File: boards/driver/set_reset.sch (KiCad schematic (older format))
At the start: 20 parts, among them Q86 MMBT2222, Q87 MMBT2907, Q88 MMBT2222, Q89 MMBT2222

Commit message: Driver board: a bit more schematic work and some initial footprint selections
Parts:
- R215, R216, R217, R218, R219, R220, R221: footprint Resistor_SMD:R_1206_3216Metric -> Resistor_SMD:R_0603_1608Metric
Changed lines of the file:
@@
 F 0 "R215" V 3795 3550 50  0000 C CNN
 F 1 "500" V 3886 3550 50  0000 C CNN
-F 2 "Resistor_SMD:R_1206_3216Metric" V 4040 3540 50  0001 C CNN
+F 2 "Resistor_SMD:R_0603_1608Metric" V 4040 3540 50  0001 C CNN
 F 3 "~" H 4000 3550 50  0001 C CNN
 	1    4000 3550
@@
 F 0 "R216" V 4595 3300 50  0000 C CNN
 F 1 "1k" V 4686 3300 50  0000 C CNN
-F 2 "Resistor_SMD:R_1206_3216Metric" V 4840 3290 50  0001 C CNN
+F 2 "Resistor_SMD:R_0603_1608Metric" V 4840 3290 50  0001 C CNN
 F 3 "~" H 4800 3300 50  0001 C CNN
 	1    4800 3300
@@
 F 0 "R217" H 5068 2946 50  0000 L CNN
 F 1 "5.1k" H 5068 2855 50  0000 L CNN
-F 2 "Resistor_SMD:R_1206_3216Metric" V 5040 2890 50  0001 C CNN
+F 2 "Resistor_SMD:R_0603_1608Metric" V 5040 2890 50  0001 C CNN
 F 3 "~" H 5000 2900 50  0001 C CNN
 	1    5000 2900
@@
 F 0 "R219" H 5968 2896 50  0000 L CNN
 F 1 "27" H 5968 2805 50  0000 L CNN
-F 2 "Resistor_SMD:R_1206_3216Metric" V 5940 2840 50  0001 C CNN
+F 2 "Resistor_SMD:R_0603_1608Metric" V 5940 2840 50  0001 C CNN
 F 3 "~" H 5900 2850 50  0001 C CNN
 	1    5900 2850
@@
 F 0 "R218" H 5118 4196 50  0000 L CNN
 F 1 "5.1k" H 5118 4105 50  0000 L CNN
-F 2 "Resistor_SMD:R_1206_3216Metric" V 5090 4140 50  0001 C CNN
+F 2 "Resistor_SMD:R_0603_1608Metric" V 5090 4140 50  0001 C CNN
 F 3 "~" H 5050 4150 50  0001 C CNN
 	1    5050 4150
@@
 F 0 "R220" H 6718 4296 50  0000 L CNN
 F 1 "NOM" H 6718 4205 50  0000 L CNN
-F 2 "Resistor_SMD:R_1206_3216Metric" V 6690 4240 50  0001 C CNN
+F 2 "Resistor_SMD:R_0603_1608Metric" V 6690 4240 50  0001 C CNN
 F 3 "~" H 6650 4250 50  0001 C CNN
 	1    6650 4250
@@
 F 0 "R221" H 7368 4146 50  0000 L CNN
 F 1 "NOM" H 7368 4055 50  0000 L CNN
-F 2 "Resistor_SMD:R_1206_3216Metric" V 7340 4090 50  0001 C CNN
+F 2 "Resistor_SMD:R_0603_1608Metric" V 7340 4090 50  0001 C CNN
 F 3 "~" H 7300 4100 50  0001 C CNN
 	1    7300 4100

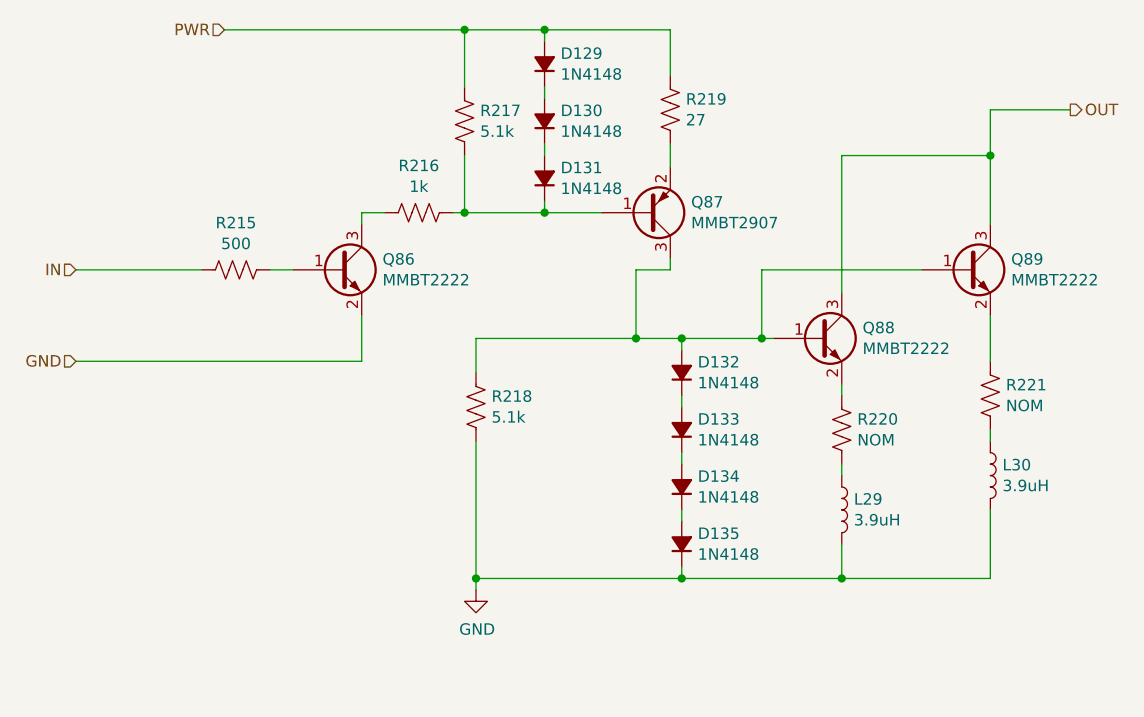
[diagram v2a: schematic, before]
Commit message: Driver board: fleshed out the hotswap controller, tweaked some resistors, and added some bypass caps
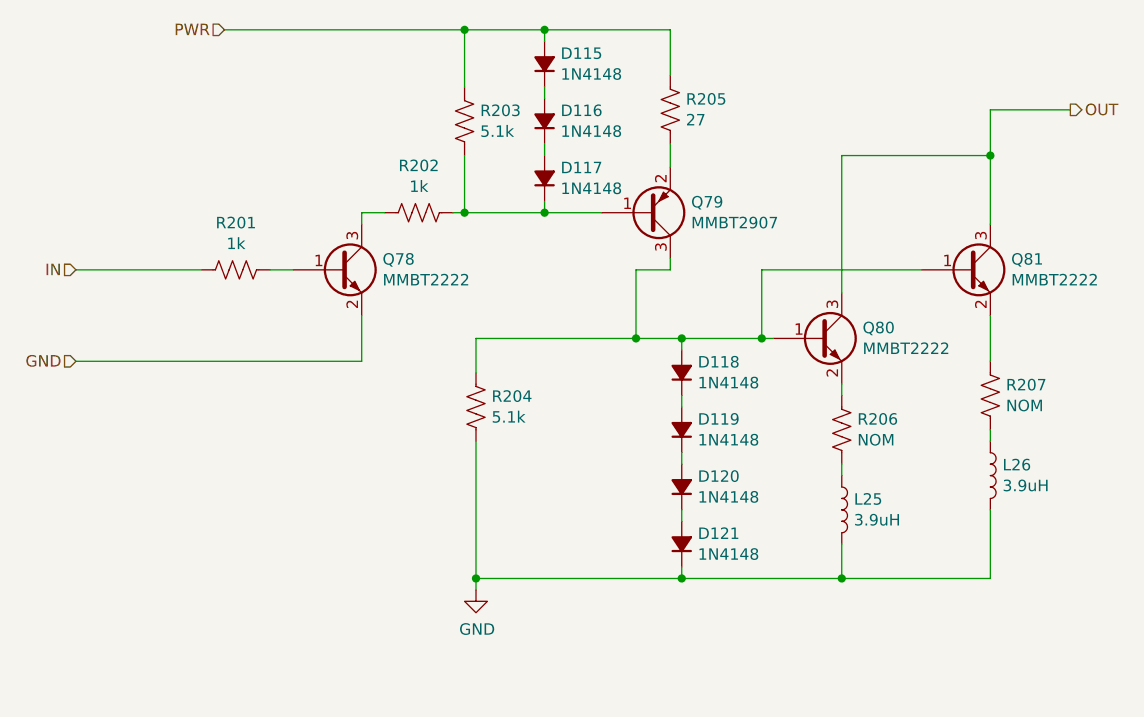
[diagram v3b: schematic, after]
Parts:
- R215: value 500 -> 1k
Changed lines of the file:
@@
 $Descr A4 11693 8268
 encoding utf-8
-Sheet 30 69
+Sheet 53 69
 Title ""
 Date ""
@@
 AR Path="/6183FAE6/623E7DB1/623343FA" Ref="R187"  Part="1"
 AR Path="/6183FAE6/623E7DC0/623343FA" Ref="R180"  Part="1"
-F 0 "R215" V 3795 3550 50  0000 C CNN
-F 1 "500" V 3886 3550 50  0000 C CNN
+F 0 "R201" V 3795 3550 50  0000 C CNN
+F 1 "1k" V 3886 3550 50  0000 C CNN
 F 2 "Resistor_SMD:R_0603_1608Metric" V 4040 3540 50  0001 C CNN
 F 3 "~" H 4000 3550 50  0001 C CNN
@@
 AR Path="/6183FAE6/623E7DB1/62336B69" Ref="Q70"  Part="1"
 AR Path="/6183FAE6/623E7DC0/62336B69" Ref="Q66"  Part="1"
-F 0 "Q86" H 4641 3596 50  0000 L CNN
+F 0 "Q78" H 4641 3596 50  0000 L CNN
 F 1 "MMBT2222" H 4641 3505 50  0000 L CNN
 F 2 "Package_TO_SOT_SMD:SOT-23" H 4650 3650 50  0001 C CNN
@@
 AR Path="/6183FAE6/623E7DB1/623392F7" Ref="R188"  Part="1"
 AR Path="/6183FAE6/623E7DC0/623392F7" Ref="R181"  Part="1"
-F 0 "R216" V 4595 3300 50  0000 C CNN
+F 0 "R202" V 4595 3300 50  0000 C CNN
 F 1 "1k" V 4686 3300 50  0000 C CNN
 F 2 "Resistor_SMD:R_0603_1608Metric" V 4840 3290 50  0001 C CNN
@@
 AR Path="/6183FAE6/623E7DB1/623399B1" Ref="R189"  Part="1"
 AR Path="/6183FAE6/623E7DC0/623399B1" Ref="R182"  Part="1"
-F 0 "R217" H 5068 2946 50  0000 L CNN
+F 0 "R203" H 5068 2946 50  0000 L CNN
 F 1 "5.1k" H 5068 2855 50  0000 L CNN
 F 2 "Resistor_SMD:R_0603_1608Metric" V 5040 2890 50  0001 C CNN
@@
 AR Path="/6183FAE6/623E7DB1/6233D2CD" Ref="D103"  Part="1"
 AR Path="/6183FAE6/623E7DC0/6233D2CD" Ref="D96"  Part="1"
-F 0 "D131" V 5396 3080 50  0000 R CNN
+F 0 "D117" V 5396 3080 50  0000 R CNN
 F 1 "1N4148" V 5305 3080 50  0000 R CNN
 F 2 "Diode_SMD:D_SOD-323" V 5350 3150 50  0001 C CNN
@@
 AR Path="/6183FAE6/623E7DB1/6233D977" Ref="D102"  Part="1"
 AR Path="/6183FAE6/623E7DC0/6233D977" Ref="D95"  Part="1"
-F 0 "D130" V 5396 2830 50  0000 R CNN
+F 0 "D116" V 5396 2830 50  0000 R CNN
 F 1 "1N4148" V 5305 2830 50  0000 R CNN
 F 2 "Diode_SMD:D_SOD-323" V 5350 2900 50  0001 C CNN
@@
 AR Path="/6183FAE6/623E7DB1/6233DD21" Ref="D101"  Part="1"
 AR Path="/6183FAE6/623E7DC0/6233DD21" Ref="D94"  Part="1"
-F 0 "D129" V 5396 2580 50  0000 R CNN
+F 0 "D115" V 5396 2580 50  0000 R CNN
 F 1 "1N4148" V 5305 2580 50  0000 R CNN
 F 2 "Diode_SMD:D_SOD-323" V 5350 2650 50  0001 C CNN
@@
 AR Path="/6183FAE6/623E7DB1/6233F700" Ref="Q71"  Part="1"
 AR Path="/6183FAE6/623E7DC0/6233F700" Ref="Q67"  Part="1"
-F 0 "Q87" H 5991 3254 50  0000 L CNN
+F 0 "Q79" H 5991 3254 50  0000 L CNN
 F 1 "MMBT2907" H 5991 3345 50  0000 L CNN
 F 2 "Package_TO_SOT_SMD:SOT-23" H 6000 3400 50  0001 C CNN
@@
 AR Path="/6183FAE6/623E7DB1/62341C10" Ref="R191"  Part="1"
 AR Path="/6183FAE6/623E7DC0/62341C10" Ref="R184"  Part="1"
-F 0 "R219" H 5968 2896 50  0000 L CNN
+F 0 "R205" H 5968 2896 50  0000 L CNN
 F 1 "27" H 5968 2805 50  0000 L CNN
 F 2 "Resistor_SMD:R_0603_1608Metric" V 5940 2840 50  0001 C CNN
@@
 AR Path="/6183FAE6/623E7DB1/62342935" Ref="D106"  Part="1"
 AR Path="/6183FAE6/623E7DC0/62342935" Ref="D99"  Part="1"
-F 0 "D134" V 5996 4430 50  0000 R CNN
+F 0 "D120" V 5996 4430 50  0000 R CNN
 F 1 "1N4148" V 5905 4430 50  0000 R CNN
 F 2 "Diode_SMD:D_SOD-323" V 5950 4500 50  0001 C CNN
@@
 AR Path="/6183FAE6/623E7DB1/6234294F" Ref="D105"  Part="1"
 AR Path="/6183FAE6/623E7DC0/6234294F" Ref="D98"  Part="1"
-F 0 "D133" V 5996 4180 50  0000 R CNN
+F 0 "D119" V 5996 4180 50  0000 R CNN
 F 1 "1N4148" V 5905 4180 50  0000 R CNN
 F 2 "Diode_SMD:D_SOD-323" V 5950 4250 50  0001 C CNN
@@
 AR Path="/6183FAE6/623E7DB1/62342959" Ref="D104"  Part="1"
 AR Path="/6183FAE6/623E7DC0/62342959" Ref="D97"  Part="1"
-F 0 "D132" V 5996 3930 50  0000 R CNN
+F 0 "D118" V 5996 3930 50  0000 R CNN
 F 1 "1N4148" V 5905 3930 50  0000 R CNN
 F 2 "Diode_SMD:D_SOD-323" V 5950 4000 50  0001 C CNN
@@
 AR Path="/6183FAE6/623E7DB1/62344A04" Ref="D107"  Part="1"
 AR Path="/6183FAE6/623E7DC0/62344A04" Ref="D100"  Part="1"
-F 0 "D135" V 5996 4680 50  0000 R CNN
+F 0 "D121" V 5996 4680 50  0000 R CNN
 F 1 "1N4148" V 5905 4680 50  0000 R CNN
 F 2 "Diode_SMD:D_SOD-323" V 5950 4750 50  0001 C CNN
@@
 AR Path="/6183FAE6/623E7DB1/6234688F" Ref="R190"  Part="1"
 AR Path="/6183FAE6/623E7DC0/6234688F" Ref="R183"  Part="1"
-F 0 "R218" H 5118 4196 50  0000 L CNN
+F 0 "R204" H 5118 4196 50  0000 L CNN
 F 1 "5.1k" H 5118 4105 50  0000 L CNN
 F 2 "Resistor_SMD:R_0603_1608Metric" V 5090 4140 50  0001 C CNN
@@
 Connection ~ 5050 4900
 $Comp
-L power:GND #PWR085
+L power:GND #PWR088
 U 1 1 62348278
 P 5050 4950
-AR Path="/6183FAE6/6232C4EF/62348278" Ref="#PWR085"  Part="1"
-AR Path="/6183FAE6/623C263E/62348278" Ref="#PWR084"  Part="1"
+AR Path="/6183FAE6/6232C4EF/62348278" Ref="#PWR088"  Part="1"
+AR Path="/6183FAE6/623C263E/62348278" Ref="#PWR087"  Part="1"
 AR Path="/6183FAE6/623D514A/62348278" Ref="#PWR?"  Part="1"
-AR Path="/6183FAE6/623D5718/62348278" Ref="#PWR083"  Part="1"
-AR Path="/6183FAE6/623DF4E1/62348278" Ref="#PWR082"  Part="1"
-AR Path="/6183FAE6/623E7DB1/62348278" Ref="#PWR081"  Part="1"
-AR Path="/6183FAE6/623E7DC0/62348278" Ref="#PWR080"  Part="1"
-F 0 "#PWR085" H 5050 4700 50  0001 C CNN
+AR Path="/6183FAE6/623D5718/62348278" Ref="#PWR086"  Part="1"
+AR Path="/6183FAE6/623DF4E1/62348278" Ref="#PWR085"  Part="1"
+AR Path="/6183FAE6/623E7DB1/62348278" Ref="#PWR084"  Part="1"
+AR Path="/6183FAE6/623E7DC0/62348278" Ref="#PWR083"  Part="1"
+F 0 "#PWR086" H 5050 4700 50  0001 C CNN
 F 1 "GND" H 5055 4777 50  0000 C CNN
 F 2 "" H 5050 4950 50  0001 C CNN
@@
 AR Path="/6183FAE6/623E7DB1/623499CA" Ref="Q72"  Part="1"
 AR Path="/6183FAE6/623E7DC0/623499CA" Ref="Q68"  Part="1"
-F 0 "Q88" H 6741 3896 50  0000 L CNN
+F 0 "Q80" H 6741 3896 50  0000 L CNN
 F 1 "MMBT2222" H 6741 3805 50  0000 L CNN
 F 2 "Package_TO_SOT_SMD:SOT-23" H 6750 3950 50  0001 C CNN
@@
 AR Path="/6183FAE6/623E7DB1/6234A8D3" Ref="Q73"  Part="1"
 AR Path="/6183FAE6/623E7DC0/6234A8D3" Ref="Q69"  Part="1"
-F 0 "Q89" H 7391 3596 50  0000 L CNN
+F 0 "Q81" H 7391 3596 50  0000 L CNN
 F 1 "MMBT2222" H 7391 3505 50  0000 L CNN
 F 2 "Package_TO_SOT_SMD:SOT-23" H 7400 3650 50  0001 C CNN
@@
 AR Path="/6183FAE6/623E7DB1/623506CE" Ref="R192"  Part="1"
 AR Path="/6183FAE6/623E7DC0/623506CE" Ref="R185"  Part="1"
-F 0 "R220" H 6718 4296 50  0000 L CNN
+F 0 "R206" H 6718 4296 50  0000 L CNN
 F 1 "NOM" H 6718 4205 50  0000 L CNN
 F 2 "Resistor_SMD:R_0603_1608Metric" V 6690 4240 50  0001 C CNN
@@
 AR Path="/6183FAE6/623E7DB1/62353148" Ref="L21"  Part="1"
 AR Path="/6183FAE6/623E7DC0/62353148" Ref="L19"  Part="1"
-F 0 "L29" H 6703 4646 50  0000 L CNN
+F 0 "L25" H 6703 4646 50  0000 L CNN
 F 1 "3.9uH" H 6703 4555 50  0000 L CNN
 F 2 "" H 6650 4600 50  0001 C CNN
@@
 AR Path="/6183FAE6/623E7DB1/6235467B" Ref="R193"  Part="1"
 AR Path="/6183FAE6/623E7DC0/6235467B" Ref="R186"  Part="1"
-F 0 "R221" H 7368 4146 50  0000 L CNN
+F 0 "R207" H 7368 4146 50  0000 L CNN
 F 1 "NOM" H 7368 4055 50  0000 L CNN
 F 2 "Resistor_SMD:R_0603_1608Metric" V 7340 4090 50  0001 C CNN
@@
 AR Path="/6183FAE6/623E7DB1/6235469A" Ref="L22"  Part="1"
 AR Path="/6183FAE6/623E7DC0/6235469A" Ref="L20"  Part="1"
-F 0 "L30" H 7353 4496 50  0000 L CNN
+F 0 "L26" H 7353 4496 50  0000 L CNN
 F 1 "3.9uH" H 7353 4405 50  0000 L CNN
 F 2 "" H 7300 4450 50  0001 C CNN

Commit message: Driver board: significant cleanup. Moved sense amp pairs into a subsheet, split tuning resistors into two globally, pushed input circuits into their corresponding sheets.
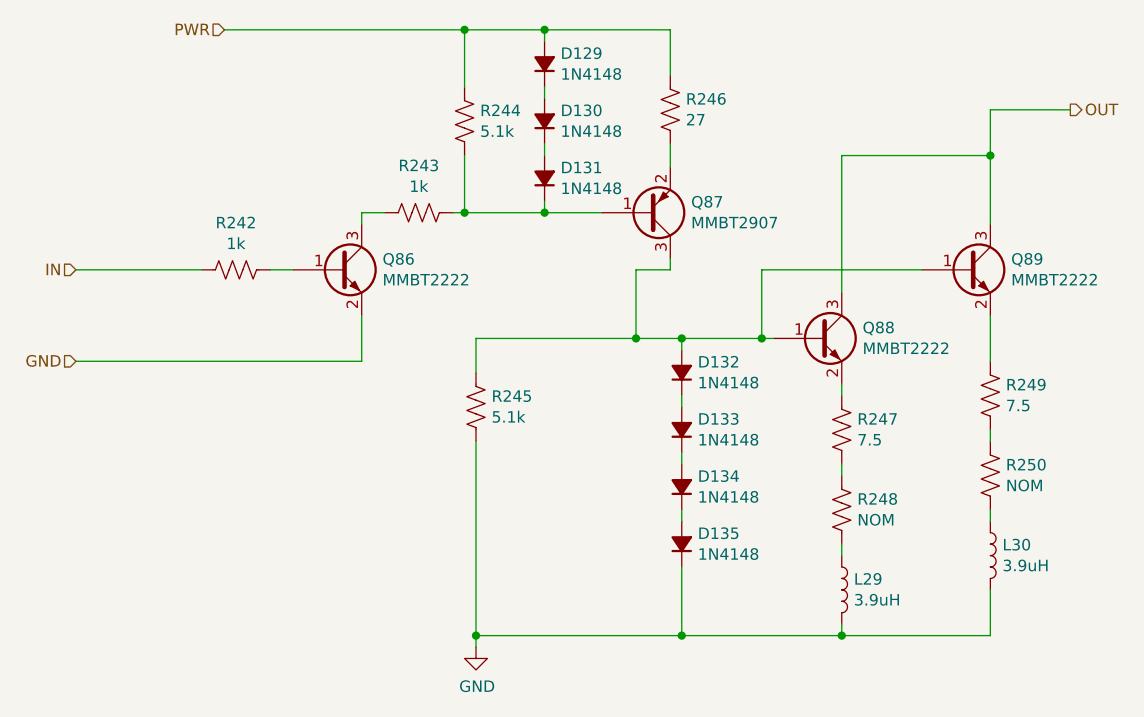
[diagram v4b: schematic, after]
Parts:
- added R248, R250: NOM, Resistor_SMD:R_0603_1608Metric, symbol Device:R_US
- L29, L30: footprint (none) -> Inductor_SMD:L_1812_4532Metric
- R247: renamed from R220; value NOM -> 7.5
- R249: renamed from R221; value NOM -> 7.5
- renumbered R215 to R242, R216 to R243, R217 to R244, R218 to R245, R219 to R246
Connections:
- net at R247.2: now also R248.1; no longer L29.1
- net at R249.2: now also R250.1; no longer L30.1
- new net: L29.1, R248.2
- new net: L30.1, R250.2
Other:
- moved on the sheet: L29, L30

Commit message: Driver board: integrated DIN 41612 backplane connector, and made a dedicated parity inhibit sheet with a different set resistor value.
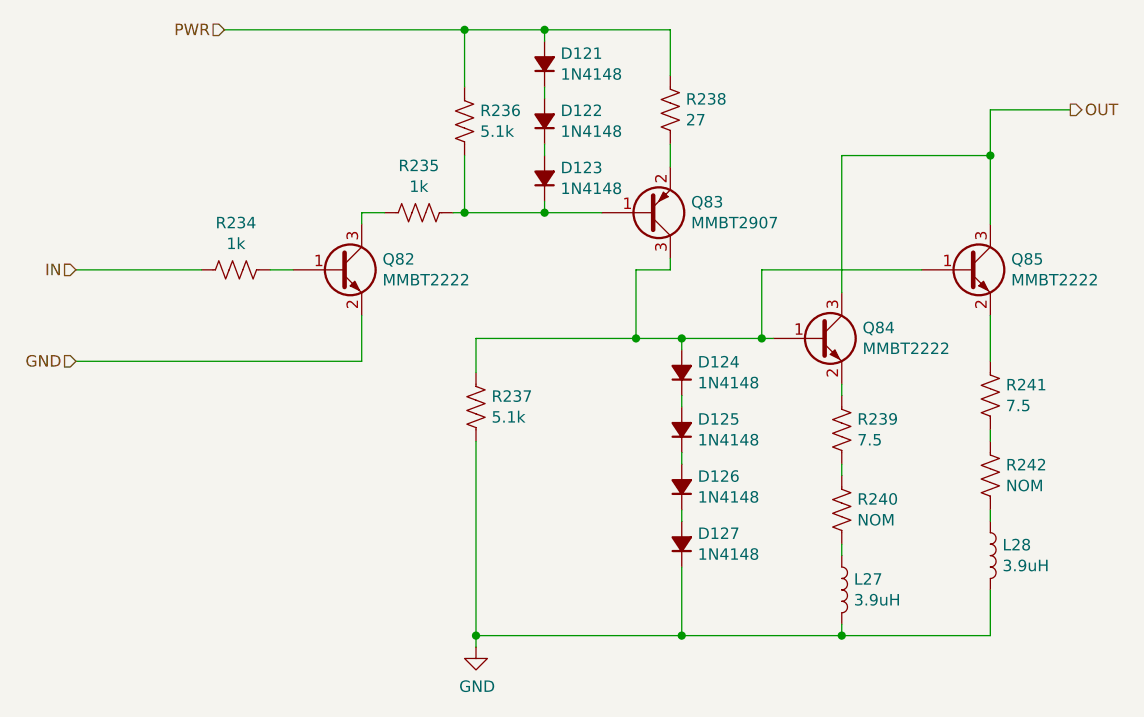
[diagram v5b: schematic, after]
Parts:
- renumbered D129 to D121, D130 to D122, D131 to D123, D132 to D124, D133 to D125, D134 to D126, D135 to D127, L29 to L27, L30 to L28, Q86 to Q82, Q87 to Q83, Q88 to Q84, Q89 to Q85, R242 to R234, R243 to R235, R244 to R236, R245 to R237, R246 to R238, R247 to R239, R248 to R240, R249 to R241, R250 to R242

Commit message: Driver board: largely fleshed out part selection
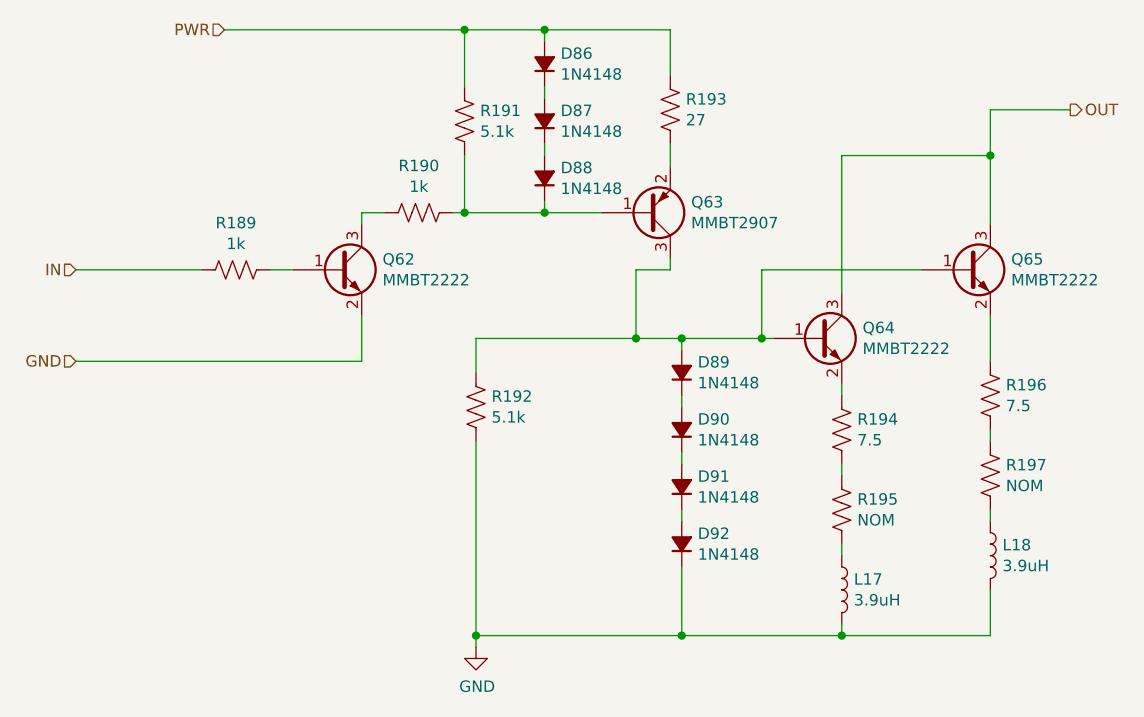
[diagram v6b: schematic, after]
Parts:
- D121, D122, D123, D124, D125, D126, D127: Digikey (none) -> https://www.digikey.com/en/products/detail/smc-diode-soluti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; Part Number (none) -> 1N4148WSTR
- L27, L28: DCR (none) -> 0.9; Digikey (none) -> https://www.digikey.com/en/products/detail/api-delevan-inc/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; Part Number (none) -> 1812R-392J; Rating (none) -> 472mA; Tolerance (none) -> 5%
- Q82, Q84, Q85: Digikey (none) -> https://www.digikey.com/en/products/detail/MMBT2222A-G/641-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; Part Number (none) -> MMBT2222A-G
- Q83: Digikey (none) -> https://www.digikey.com/en/products/detail/MMBT2907A-G/641-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; Part Number (none) -> MMBT2907A-G
- R239, R241: footprint Resistor_SMD:R_0603_1608Metric -> Resistor_SMD:R_0805_2012Metric
